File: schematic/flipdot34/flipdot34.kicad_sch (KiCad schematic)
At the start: 4 parts, among them J1 Conn_02x17_Odd_Even, U1 74HC595, U2 74HC595

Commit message: Schematic - add communication and config connectors
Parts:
- added C1, C2, C4: 100n, symbol Device:C_Small
- added C3: 100m, symbol Device:C_Polarized_Small
- added J2: (no value), symbol Connector_Generic:Conn_02x05_Odd_Even
- added J3: (no value), symbol Connector_Generic:Conn_02x03_Odd_Even
- J1: value Conn_02x17_Odd_Even -> J1
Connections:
- net +5V: now also C1.2, C2.2, C3.1, C4.1, J2.7 (Pin_7), J2.9 (Pin_9)
- net A0-X: now also U1.15 (QA)
- net A0-Y: now also U2.15 (QA)
- net A1-X: now also U1.1 (QB)
- net A1-Y: now also U2.1 (QB)
- net A2-X: now also U1.2 (QC)
- net A2-Y: now also U2.2 (QC)
- net B0-X: now also U1.3 (QD)
- net B0-Y: now also U2.3 (QD)
- net B1-X: now also U1.4 (QE)
- net B1-Y: now also U2.4 (QE)
- net DATA-X: now also U1.5 (QF)
- net ENABLE-X-6: now also J1.28 (Pin_28)
- net ENABLE-Y-RESET: now also U1.7 (QH)
- net ENABLE-Y-SET: now also U1.6 (QG)
- net GND: now also J1.31 (Pin_31), J1.32 (Pin_32), J1.33 (Pin_33), J1.34 (Pin_34), C1.1, C2.1, C3.2, C4.2, J2.10 (Pin_10), J2.2 (Pin_2), J2.4 (Pin_4), J2.6 (Pin_6), J2.8 (Pin_8), J3.2 (Pin_2), J3.4 (Pin_4), J3.6 (Pin_6)
- net at U1.12 (RCLK), U2.12 (RCLK): now also A1.15 (D12); no longer A1.12 (D9)
- net ENABLE-X-8: now reaches J1.26 (Pin_26)
- net ENABLE-X-8: now also A1.12 (D9)
- net ENABLE-X-7: now reaches A1.11 (D8)
- net CFG-0: now reaches A1.19 (A0)
- net CFG-0: now also J3.1 (Pin_1)
- net CFG-1: now reaches A1.20 (A1)
- net CFG-1: now also J3.3 (Pin_3)
- net CFG-2: now reaches A1.21 (A2)
- net CFG-2: now also J3.5 (Pin_5)
- net SDA: now reaches A1.23 (A4)
- net SDA: now also J2.1 (Pin_1)
- net SCL: now reaches A1.24 (A5)
- net SCL: now also J2.3 (Pin_3)
- net RESET: now reaches A1.3 (~{RESET})
- net RESET: now also J2.5 (Pin_5)
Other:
- moved on the sheet: J1, U2

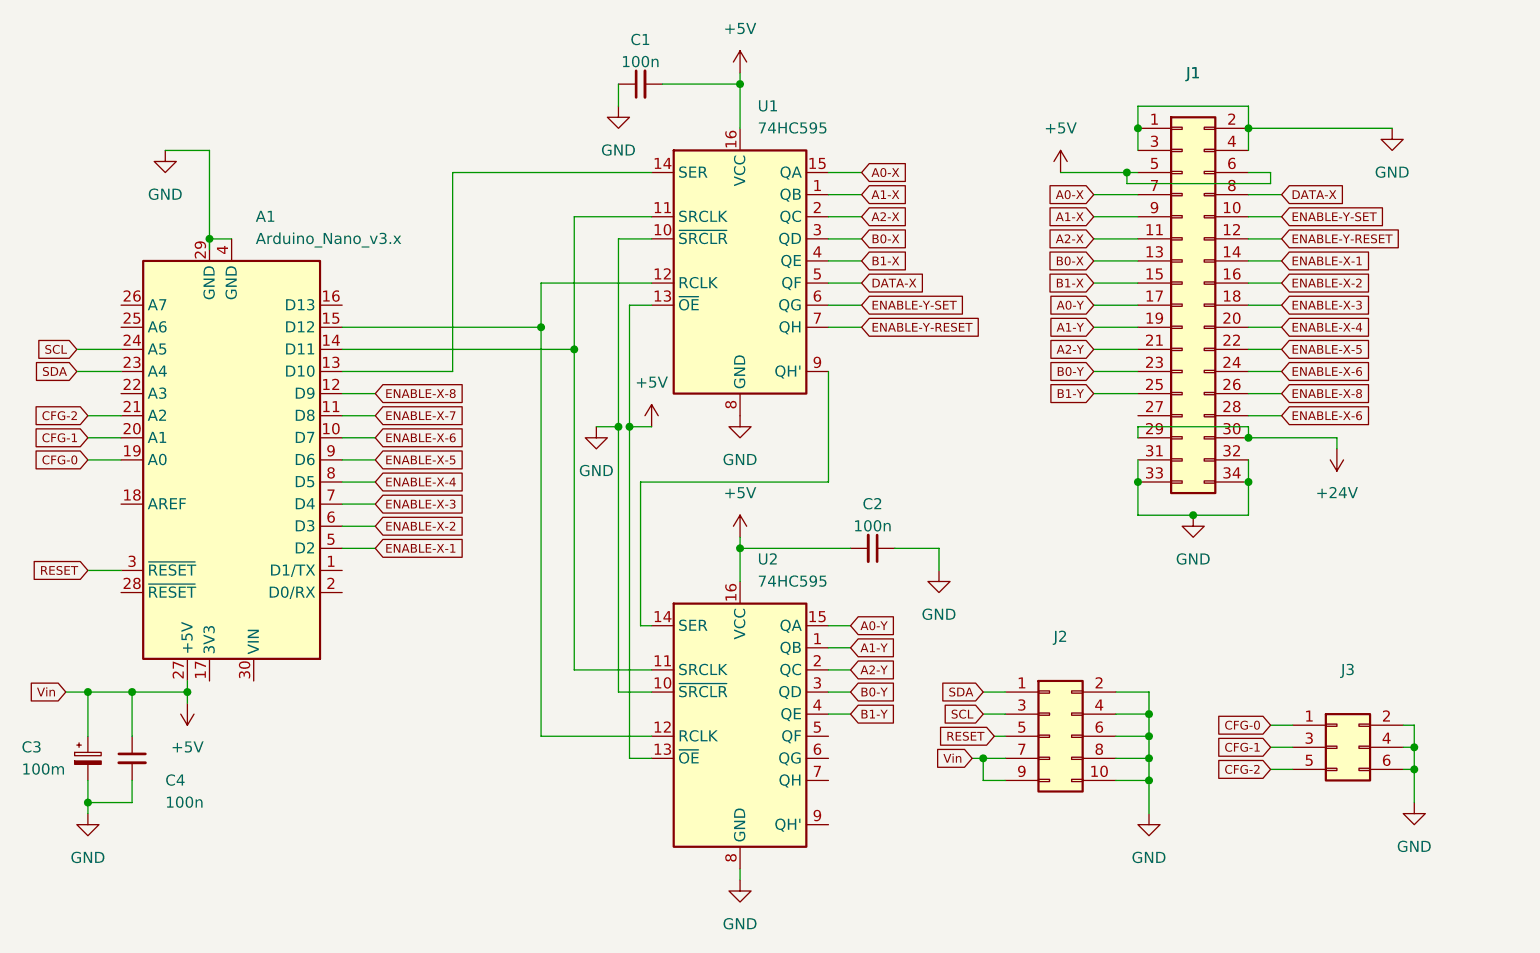
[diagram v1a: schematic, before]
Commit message: Add +24V terminal
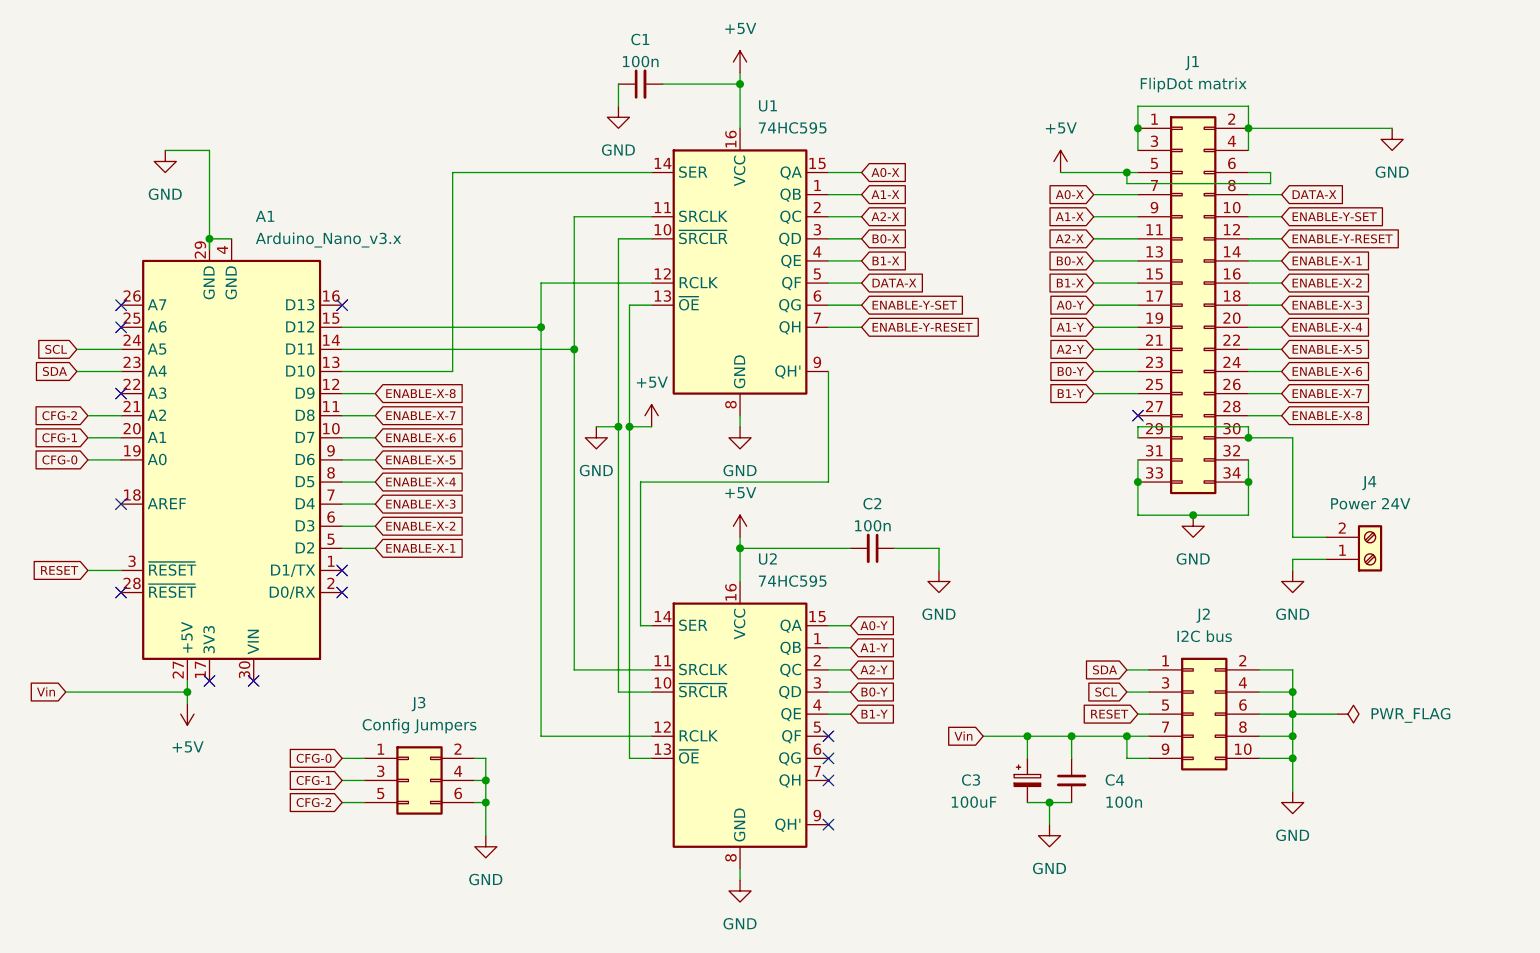
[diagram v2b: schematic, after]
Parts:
- added J4: Power 24V, symbol Connector:Screw_Terminal_01x02
- C3: value 100m -> 100uF
- J1: value J1 -> FlipDot matrix
- J2: value (none) -> I2C bus
- J3: value (none) -> Config Jumpers
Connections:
- net ENABLE-X-6: no longer J1.28 (Pin_28)
- net ENABLE-X-7: now also J1.26 (Pin_26)
- net ENABLE-X-8: now also J1.28 (Pin_28); no longer J1.26 (Pin_26)
- net GND: now also J4.1 (Pin_1)
- net +24V: no longer names the net of J1.29 (Pin_29), J1.30 (Pin_30)
- net +24V: now also J4.2 (Pin_2)
- no-connect marks 0 -> 15
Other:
- moved on the sheet: C3, C4, J2, J3

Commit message: Assign footprints
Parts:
- C1, C2, C4: footprint (none) -> Capacitor_THT:C_Disc_D5.0mm_W2.5mm_P5.00mm
- C3: footprint (none) -> Capacitor_THT:CP_Radial_D6.3mm_P2.50mm
- J1: footprint (none) -> Connector_IDC:IDC-Header_2x17_P2.54mm_Vertical
- J2: footprint (none) -> Connector_IDC:IDC-Header_2x05_P2.54mm_Vertical
- J3: footprint (none) -> Connector_PinHeader_2.54mm:PinHeader_2x03_P2.54mm_Vertical
- J4: footprint (none) -> TerminalBlock:TerminalBlock_bornier-2_P5.08mm
- U1, U2: footprint (none) -> Package_DIP:DIP-16_W7.62mm_LongPads
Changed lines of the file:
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@@
       (effects (font (size 1.27 1.27)) (justify left))
     )
-    (property "Footprint" "" (id 2) (at 113.03 52.07 0)
+    (property "Footprint" "Package_DIP:DIP-16_W7.62mm_LongPads" (id 2) (at 113.03 52.07 0)
       (effects (font (size 1.27 1.27)) hide)
     )
@@
       (effects (font (size 1.27 1.27)) (justify left))
     )
-    (property "Footprint" "" (id 2) (at 146.05 111.76 0)
+    (property "Footprint" "Capacitor_THT:CP_Radial_D6.3mm_P2.50mm" (id 2) (at 146.05 111.76 0)
       (effects (font (size 1.27 1.27)) hide)
     )
@@
     (property "Reference" "J1" (id 0) (at 165.1 29.21 0))
     (property "Value" "FlipDot matrix" (id 1) (at 165.1 31.75 0))
-    (property "Footprint" "" (id 2) (at 163.83 57.15 0)
+    (property "Footprint" "Connector_IDC:IDC-Header_2x17_P2.54mm_Vertical" (id 2) (at 163.83 57.15 0)
       (effects (font (size 1.27 1.27)) hide)
     )
@@
       (effects (font (size 1.27 1.27)) (justify left))
     )
-    (property "Footprint" "" (id 2) (at 151.13 111.76 0)
+    (property "Footprint" "Capacitor_THT:C_Disc_D5.0mm_W2.5mm_P5.00mm" (id 2) (at 151.13 111.76 0)
       (effects (font (size 1.27 1.27)) hide)
     )
@@
     (property "Reference" "J3" (id 0) (at 76.2 102.87 0))
     (property "Value" "Config Jumpers" (id 1) (at 76.2 105.41 0))
-    (property "Footprint" "" (id 2) (at 74.93 111.76 0)
+    (property "Footprint" "Connector_PinHeader_2.54mm:PinHeader_2x03_P2.54mm_Vertical" (id 2) (at 74.93 111.76 0)
       (effects (font (size 1.27 1.27)) hide)
     )
@@
       (effects (font (size 1.27 1.27)) (justify left))
     )
-    (property "Footprint" "" (id 2) (at 113.03 104.14 0)
+    (property "Footprint" "Package_DIP:DIP-16_W7.62mm_LongPads" (id 2) (at 113.03 104.14 0)
       (effects (font (size 1.27 1.27)) hide)
     )
@@
     (property "Reference" "J2" (id 0) (at 166.37 92.71 0))
     (property "Value" "I2C bus" (id 1) (at 166.37 95.25 0))
-    (property "Footprint" "" (id 2) (at 165.1 104.14 0)
+    (property "Footprint" "Connector_IDC:IDC-Header_2x05_P2.54mm_Vertical" (id 2) (at 165.1 104.14 0)
       (effects (font (size 1.27 1.27)) hide)
     )
@@
     (property "Reference" "C1" (id 0) (at 101.6 26.67 90))
     (property "Value" "100n" (id 1) (at 101.6 29.21 90))
-    (property "Footprint" "" (id 2) (at 101.6 31.75 0)
+    (property "Footprint" "Capacitor_THT:C_Disc_D5.0mm_W2.5mm_P5.00mm" (id 2) (at 101.6 31.75 0)
       (effects (font (size 1.27 1.27)) hide)
     )
@@
     (property "Reference" "J4" (id 0) (at 185.42 77.47 0))
     (property "Value" "Power 24V" (id 1) (at 185.42 80.01 0))
-    (property "Footprint" "" (id 2) (at 185.42 86.36 0)
+    (property "Footprint" "TerminalBlock:TerminalBlock_bornier-2_P5.08mm" (id 2) (at 185.42 86.36 0)
       (effects (font (size 1.27 1.27)) hide)
     )
@@
     (property "Reference" "C2" (id 0) (at 128.27 80.01 90))
     (property "Value" "100n" (id 1) (at 128.27 82.55 90))
-    (property "Footprint" "" (id 2) (at 128.27 85.09 0)
+    (property "Footprint" "Capacitor_THT:C_Disc_D5.0mm_W2.5mm_P5.00mm" (id 2) (at 128.27 85.09 0)
       (effects (font (size 1.27 1.27)) hide)
     )
@@
     )
     (path "/94b7b290-4e03-4b92-9cba-5683398b2561"
-      (reference "C1") (unit 1) (value "100n") (footprint "")
+      (reference "C1") (unit 1) (value "100n") (footprint "Capacitor_THT:C_Disc_D5.0mm_W2.5mm_P5.00mm")
     )
     (path "/db469775-6414-434b-86d4-b8cfbaae6f26"
-      (reference "C2") (unit 1) (value "100n") (footprint "")
+      (reference "C2") (unit 1) (value "100n") (footprint "Capacitor_THT:C_Disc_D5.0mm_W2.5mm_P5.00mm")
     )
     (path "/257839d7-7f0e-4240-9d05-81d11e0f2236"
-      (reference "C3") (unit 1) (value "100uF") (footprint "")
+      (reference "C3") (unit 1) (value "100uF") (footprint "Capacitor_THT:CP_Radial_D6.3mm_P2.50mm")
     )
     (path "/6147f979-29f6-4d1a-acc7-1b1c29a6f8c8"
-      (reference "C4") (unit 1) (value "100n") (footprint "")
+      (reference "C4") (unit 1) (value "100n") (footprint "Capacitor_THT:C_Disc_D5.0mm_W2.5mm_P5.00mm")
     )
     (path "/51498787-d262-4042-a222-87c9237f3cab"
-      (reference "J1") (unit 1) (value "FlipDot matrix") (footprint "")
+      (reference "J1") (unit 1) (value "FlipDot matrix") (footprint "Connector_IDC:IDC-Header_2x17_P2.54mm_Vertical")
     )
     (path "/89f91d5b-9c66-4a85-8b7c-91158c2b9d8d"
-      (reference "J2") (unit 1) (value "I2C bus") (footprint "")
+      (reference "J2") (unit 1) (value "I2C bus") (footprint "Connector_IDC:IDC-Header_2x05_P2.54mm_Vertical")
     )
     (path "/76512b85-5d05-464f-ae06-762d07c02178"
-      (reference "J3") (unit 1) (value "Config Jumpers") (footprint "")
+      (reference "J3") (unit 1) (value "Config Jumpers") (footprint "Connector_PinHeader_2.54mm:PinHeader_2x03_P2.54mm_Vertical")
     )
     (path "/b63e0ecd-1d73-4890-b73d-41a0791d02d8"
-      (reference "J4") (unit 1) (value "Power 24V") (footprint "")
+      (reference "J4") (unit 1) (value "Power 24V") (footprint "TerminalBlock:TerminalBlock_bornier-2_P5.08mm")
     )
     (path "/0ad88b14-75ca-4fe9-9bb6-f5d58fe3e7f9"
-      (reference "U1") (unit 1) (value "74HC595") (footprint "")
+      (reference "U1") (unit 1) (value "74HC595") (footprint "Package_DIP:DIP-16_W7.62mm_LongPads")
     )
     (path "/8170ec21-5c39-4bdb-96fa-8a9ff34993a5"
-      (reference "U2") (unit 1) (value "74HC595") (footprint "")
-    )
-  )
+      (reference "U2") (unit 1) (value "74HC595") (footprint "Package_DIP:DIP-16_W7.62mm_LongPads")
+    )
+  )

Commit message: Add board dimensions
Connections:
- net A0-X: now also U1.4 (QE); no longer U1.15 (QA)
- net A0-Y: now also U2.7 (QH); no longer U2.15 (QA)
- net A1-X: now also U1.3 (QD); no longer U1.1 (QB)
- net A1-Y: now also U2.6 (QG); no longer U2.1 (QB)
- net A2-Y: now also U2.5 (QF); no longer U2.2 (QC)
- net B0-X: now also U1.1 (QB); no longer U1.3 (QD)
- net B0-Y: now also U2.4 (QE); no longer U2.3 (QD)
- net B1-X: now also U1.15 (QA); no longer U1.4 (QE)
- net B1-Y: now also U2.3 (QD); no longer U2.4 (QE)
- net CFG-0: now also J3.5 (Pin_5); no longer J3.1 (Pin_1)
- net CFG-2: now also J3.1 (Pin_1); no longer J3.5 (Pin_5)
- net GND: now also J4.2 (Pin_2); no longer J4.1 (Pin_1)
- net RESET: now also J2.1 (Pin_1); no longer J2.5 (Pin_5)
- net SCL: now also J2.5 (Pin_5); no longer J2.3 (Pin_3)
- net SDA: now also J2.3 (Pin_3); no longer J2.1 (Pin_1)
- net at J1.29 (Pin_29), J1.30 (Pin_30): now also J4.1 (Pin_1); no longer J4.2 (Pin_2)
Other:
- moved on the sheet: J3

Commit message: Add mounting holes
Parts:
- added H1, H2, H3, H4: MountingHole, MountingHole:MountingHole_3.2mm_M3, symbol Mechanical:MountingHole
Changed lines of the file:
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@@
     (pin "1")
+  )
+  (symbol (lib_name "MountingHole_1") (lib_id "Mechanical:MountingHole") (at 189.23 125.73 0) (unit 1)
+    (in_bom no) (on_board yes) (fields_autoplaced)
+    (property "Reference" "H4" (id 0) (at 191.77 124.4599 0)
+      (effects (font (size 1.27 1.27)) (justify left))
+    )
+    (property "Value" "MountingHole" (id 1) (at 191.77 126.9999 0)
+      (effects (font (size 1.27 1.27)) (justify left) hide)
+    )
+    (property "Footprint" "MountingHole:MountingHole_3.2mm_M3" (id 2) (at 189.23 125.73 0)
+      (effects (font (size 1.27 1.27)) hide)
+    )
+    (property "Datasheet" "~" (id 3) (at 189.23 125.73 0)
+      (effects (font (size 1.27 1.27)) hide)
+    )
   )
   (symbol (lib_id "power:GND") (at 148.59 116.84 0) (unit 1)
@@
     )
     (pin "1")
+  )
+  (symbol (lib_name "MountingHole_1") (lib_id "Mechanical:MountingHole") (at 173.99 125.73 0) (unit 1)
+    (in_bom no) (on_board yes) (fields_autoplaced)
+    (property "Reference" "H2" (id 0) (at 176.53 124.4599 0)
+      (effects (font (size 1.27 1.27)) (justify left))
+    )
+    (property "Value" "MountingHole" (id 1) (at 176.53 126.9999 0)
+      (effects (font (size 1.27 1.27)) (justify left) hide)
+    )
+    (property "Footprint" "MountingHole:MountingHole_3.2mm_M3" (id 2) (at 173.99 125.73 0)
+      (effects (font (size 1.27 1.27)) hide)
+    )
+    (property "Datasheet" "~" (id 3) (at 173.99 125.73 0)
+      (effects (font (size 1.27 1.27)) hide)
+    )
   )
   (symbol (lib_id "power:GND") (at 135.89 87.63 0) (unit 1)
@@
     (pin "2")
   )
+  (symbol (lib_name "MountingHole_1") (lib_id "Mechanical:MountingHole") (at 166.37 125.73 0) (unit 1)
+    (in_bom no) (on_board yes) (fields_autoplaced)
+    (property "Reference" "H1" (id 0) (at 168.91 124.4599 0)
+      (effects (font (size 1.27 1.27)) (justify left))
+    )
+    (property "Value" "MountingHole" (id 1) (at 168.91 126.9999 0)
+      (effects (font (size 1.27 1.27)) (justify left) hide)
+    )
+    (property "Footprint" "MountingHole:MountingHole_3.2mm_M3" (id 2) (at 166.37 125.73 0)
+      (effects (font (size 1.27 1.27)) hide)
+    )
+    (property "Datasheet" "~" (id 3) (at 166.37 125.73 0)
+      (effects (font (size 1.27 1.27)) hide)
+    )
+  )
   (symbol (lib_id "power:PWR_FLAG") (at 181.61 104.14 270) (unit 1)
     (in_bom yes) (on_board yes) (fields_autoplaced)
@@
     )
     (pin "1")
+  )
+  (symbol (lib_name "MountingHole_1") (lib_id "Mechanical:MountingHole") (at 181.61 125.73 0) (unit 1)
+    (in_bom no) (on_board yes) (fields_autoplaced)
+    (property "Reference" "H3" (id 0) (at 184.15 124.4599 0)
+      (effects (font (size 1.27 1.27)) (justify left))
+    )
+    (property "Value" "MountingHole" (id 1) (at 184.15 126.9999 0)
+      (effects (font (size 1.27 1.27)) (justify left) hide)
+    )
+    (property "Footprint" "MountingHole:MountingHole_3.2mm_M3" (id 2) (at 181.61 125.73 0)
+      (effects (font (size 1.27 1.27)) hide)
+    )
+    (property "Datasheet" "~" (id 3) (at 181.61 125.73 0)
+      (effects (font (size 1.27 1.27)) hide)
+    )
   )
   (sheet_instances
@@
       (reference "C4") (unit 1) (value "100n") (footprint "Capacitor_THT:C_Disc_D5.0mm_W2.5mm_P5.00mm")
     )
+    (path "/e8530ead-dfd3-493b-9a95-dadf905bde55"
+      (reference "H1") (unit 1) (value "MountingHole") (footprint "MountingHole:MountingHole_3.2mm_M3")
+    )
+    (path "/4c237919-3273-4e71-99cd-a47bd71fdf79"
+      (reference "H2") (unit 1) (value "MountingHole") (footprint "MountingHole:MountingHole_3.2mm_M3")
+    )
+    (path "/fe25768b-9517-416a-bbe6-b2792a74c175"
+      (reference "H3") (unit 1) (value "MountingHole") (footprint "MountingHole:MountingHole_3.2mm_M3")
+    )
+    (path "/33872e56-5db0-49c0-b9da-29ead17f3c7e"
+      (reference "H4") (unit 1) (value "MountingHole") (footprint "MountingHole:MountingHole_3.2mm_M3")
+    )
     (path "/51498787-d262-4042-a222-87c9237f3cab"

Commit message: DRC tests pass
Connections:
- net A0-X: now also U2.4 (QE); no longer U1.4 (QE)
- net A0-Y: now also U1.7 (QH); no longer U2.7 (QH)
- net A1-X: now also U2.3 (QD); no longer U1.3 (QD)
- net A1-Y: now also U1.6 (QG); no longer U2.6 (QG)
- net A2-X: now also U2.2 (QC); no longer U1.2 (QC)
- net A2-Y: now also U1.5 (QF); no longer U2.5 (QF)
- net B0-X: now also U2.1 (QB); no longer U1.1 (QB)
- net B0-Y: now also U1.4 (QE); no longer U2.4 (QE)
- net B1-X: now also U2.15 (QA); no longer U1.15 (QA)
- net B1-Y: now also U1.3 (QD); no longer U2.3 (QD)
- net DATA-X: now also U2.5 (QF); no longer U1.5 (QF)
- net ENABLE-Y-RESET: now also U2.7 (QH); no longer U1.7 (QH)
- net ENABLE-Y-SET: now also U2.6 (QG); no longer U1.6 (QG)
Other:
- moved on the sheet: C3, C4, J2

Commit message: Minor fixes
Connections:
- net A0-Y: now also U1.6 (QG); no longer U1.7 (QH)
- net A1-Y: now also U1.5 (QF); no longer U1.6 (QG)
- net A2-Y: now also U1.4 (QE); no longer U1.5 (QF)
- net B0-Y: now also U1.3 (QD); no longer U1.4 (QE)
- net B1-X: now also U1.7 (QH); no longer U2.15 (QA)
- net B1-Y: now also U1.2 (QC); no longer U1.3 (QD)
